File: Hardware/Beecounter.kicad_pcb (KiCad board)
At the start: 2 copper layers, 171 parts, among them J1 Conn_01x03, J10 Conn_01x03, J11 Conn_01x03, J12 Conn_01x03, J13 Conn_01x03, J14 Conn_01x03, J15 Conn_02x20_Odd_Even, J16 Conn_01x04, J17 Conn_01x10, J2 Conn_01x03, J3 Conn_01x03, J4 Conn_01x03, J5 Conn_01x03, J6 Conn_01x03, J7 Conn_01x03, J8 Conn_01x03, J9 Conn_01x03, U1 LM393, U10 LM393, U11 H2010, U12 LM393, U13 H2010, U14 LM393, U15 H2010, U16 LM393, U17 H2010, U18 LM393, U19 H2010, U2 H2010, U20 LM393, U21 H2010, U22 LM393, U23 H2010, U24 LM393, U25 H2010, U26 LM393, U27 H2010, U28 LM393, U3 H2010, U4 LM393, U5 H2010, U6 LM393, U7 H2010, U8 LM393, U9 H2010

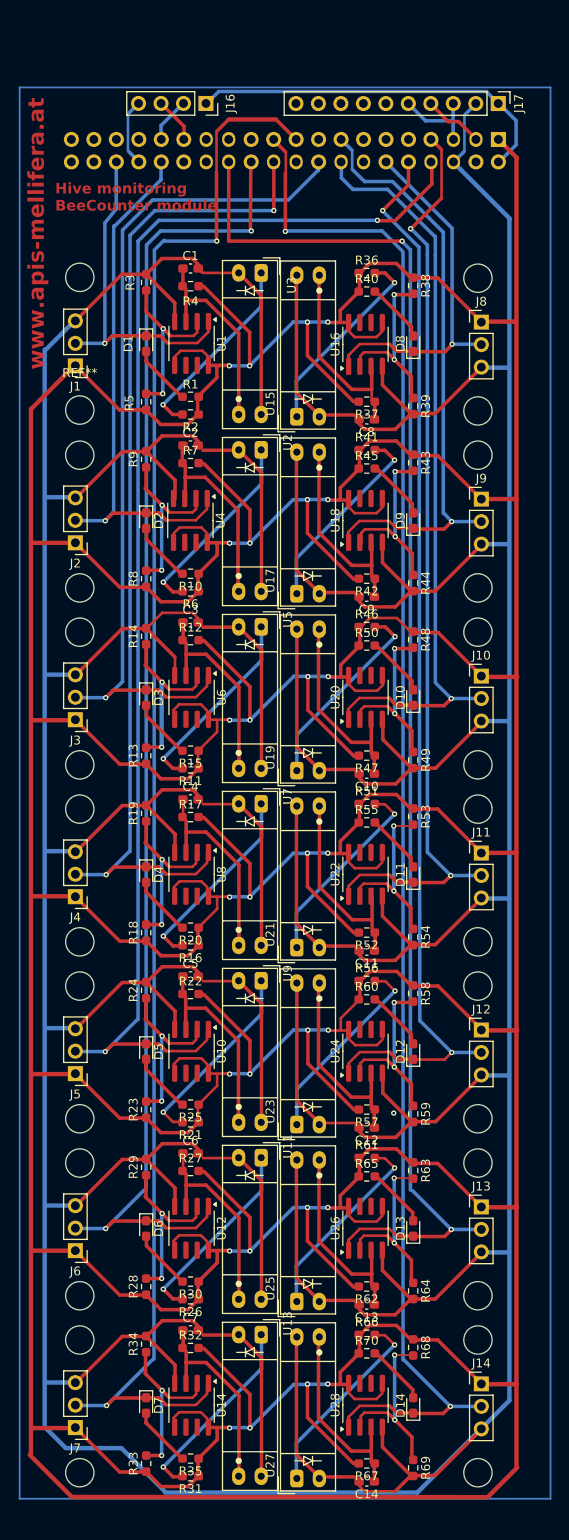
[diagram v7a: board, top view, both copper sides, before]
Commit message: Smaller outer boarders
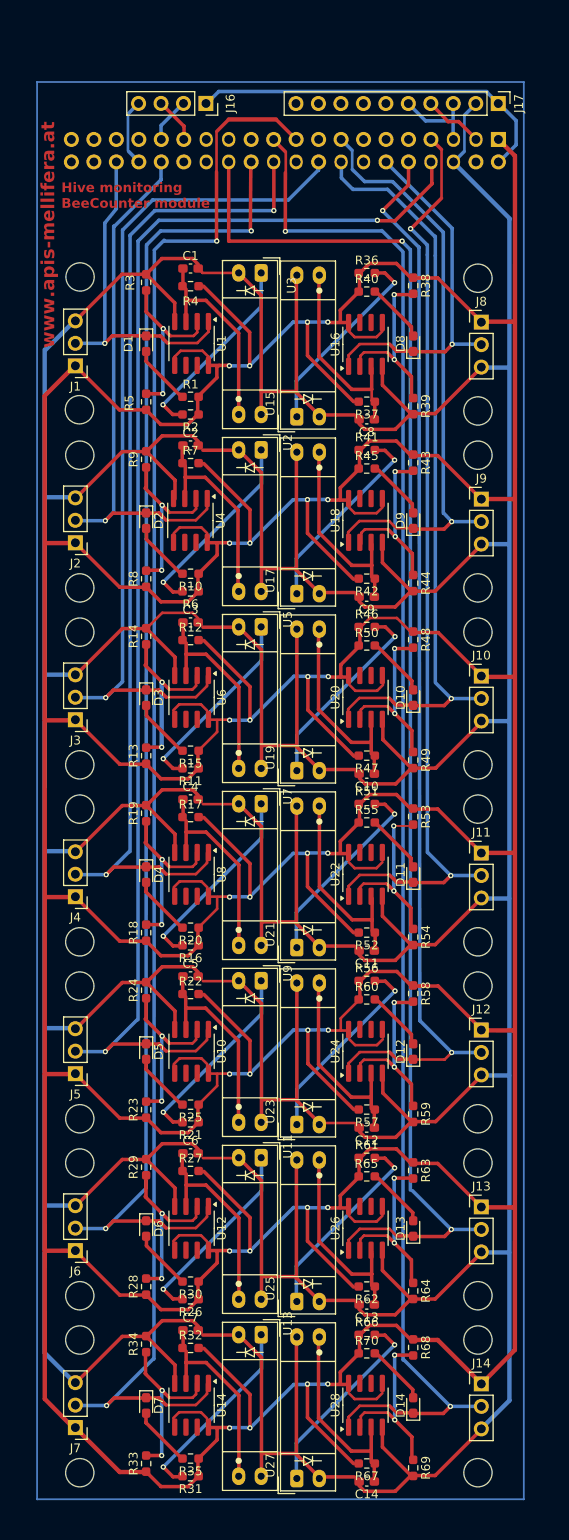
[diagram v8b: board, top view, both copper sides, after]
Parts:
- removed REF** (x2): MountingHole_3.2mm_M3, MountingHole:MountingHole_3.2mm_M3
- added ?: , , F.Cu at (42.5, 77.4)
- added ?: , , F.Cu at (42.6, 62.4)
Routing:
- net GND: track 629.5 -> 656.8 mm
- net Net-(R21-Pad2): vias 2 -> 1
